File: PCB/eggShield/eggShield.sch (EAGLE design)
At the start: 34 parts, among them U1 V_REG_LDOSMD, U2 V_REG_LDOSMD

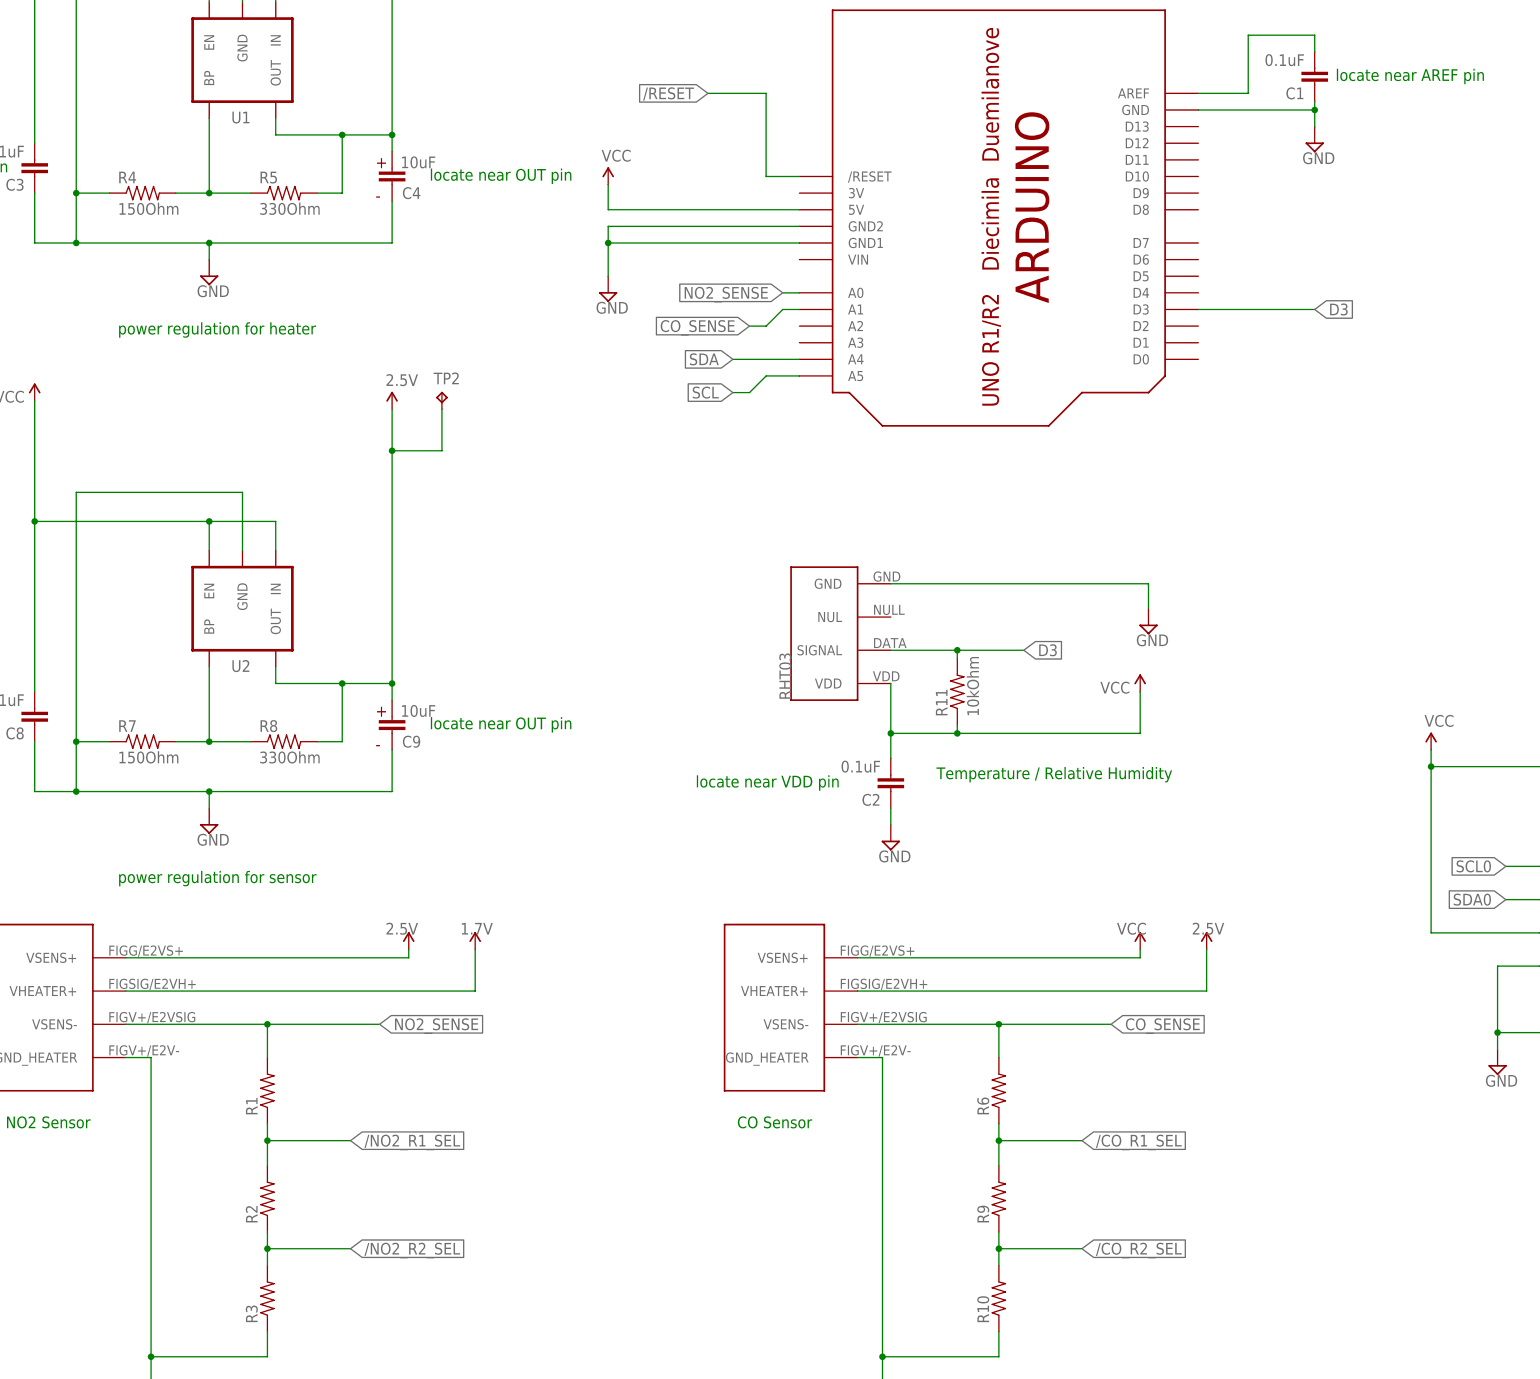
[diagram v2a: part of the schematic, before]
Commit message: added routing for range select signals to arduino header and updated silkscreen for e2v sensors
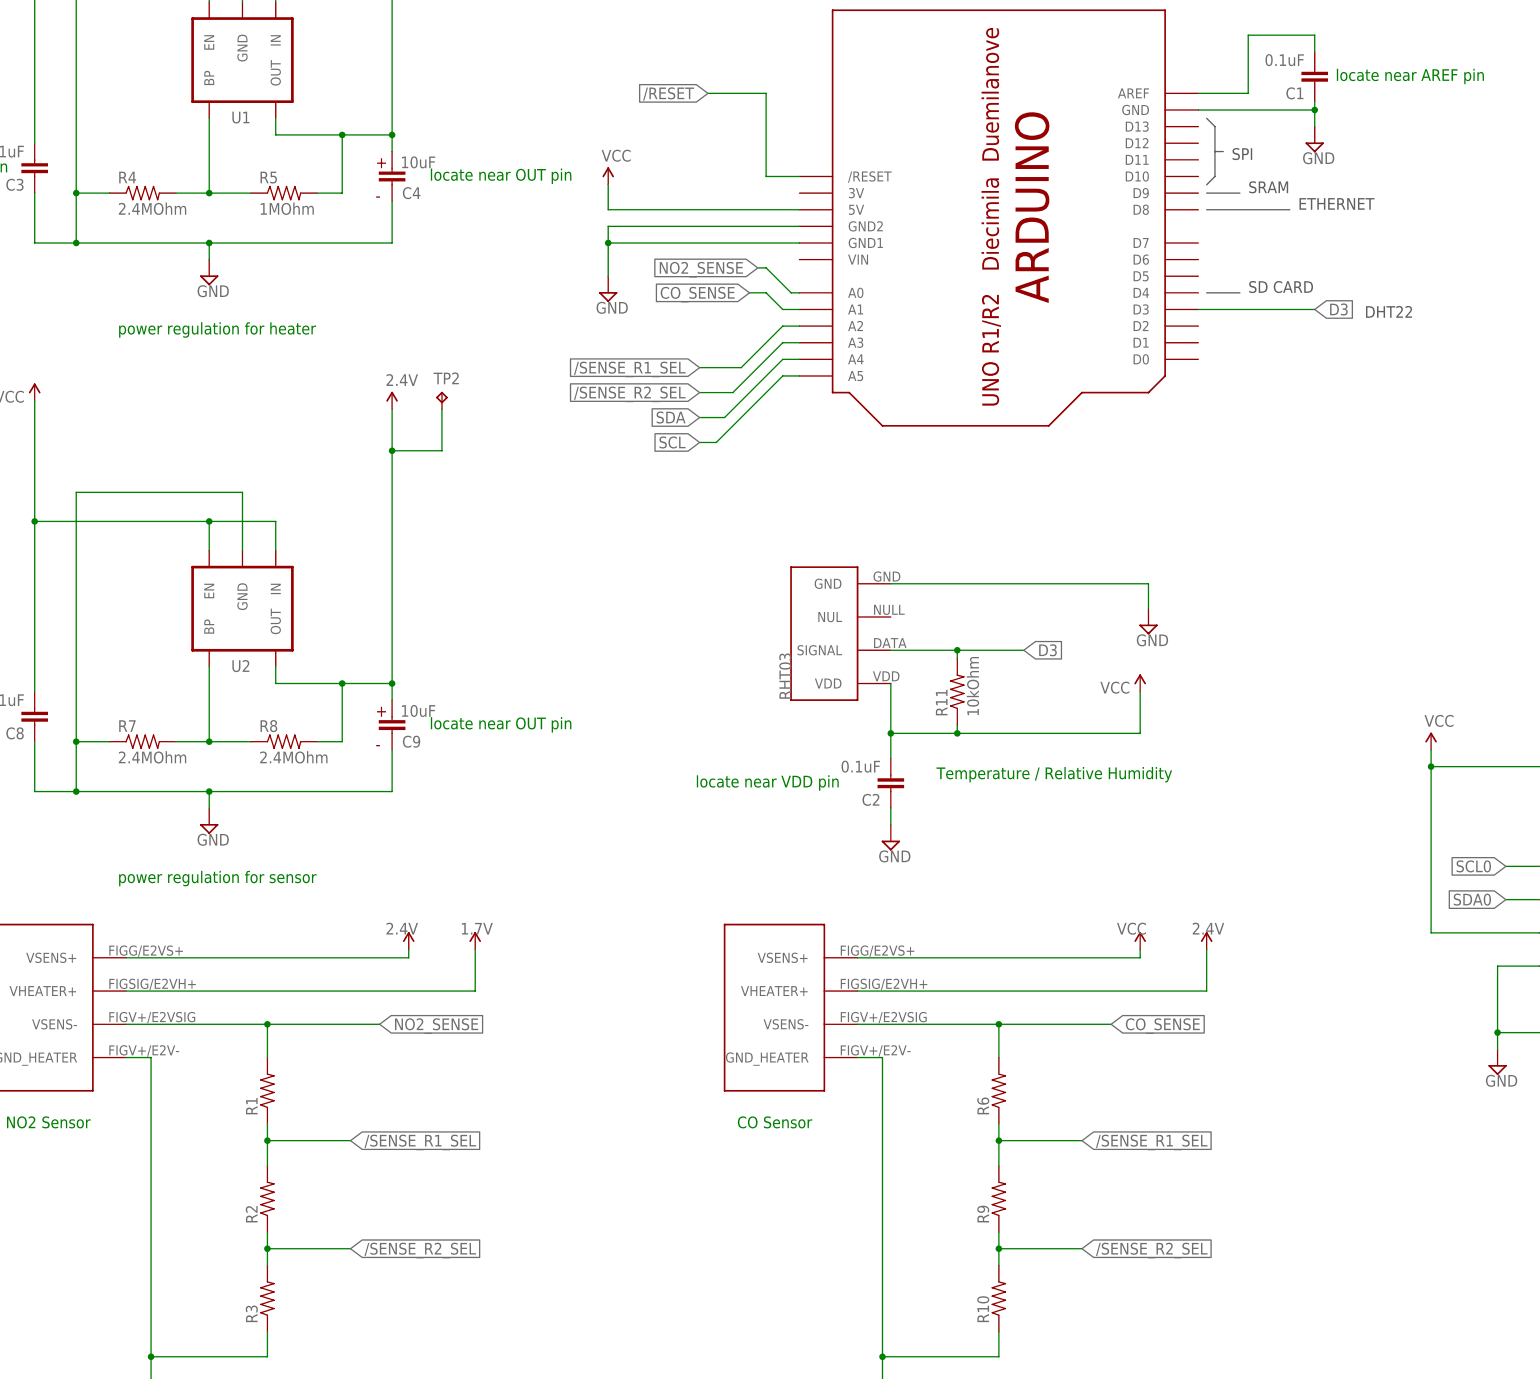
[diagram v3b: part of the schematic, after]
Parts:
- R4, R7: value 150Ohm -> 2.4MOhm
- R5: value 330Ohm -> 1MOhm
- R8: value 330Ohm -> 2.4MOhm
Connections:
- net 2.5V renamed 2.4V
- removed net /CO_R1_SEL: R6.1, R9.2
- removed net /CO_R2_SEL: R10.2, R9.1
- removed net /NO2_R1_SEL: R1.1, R2.2
- removed net /NO2_R2_SEL: R2.1, R3.2
- new net /SENSE_R1_SEL: R1.1, R2.2, R6.1, R9.2, U$7.A2
- new net /SENSE_R2_SEL: R10.2, R2.1, R3.2, R9.1, U$7.A3
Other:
- note added: "DHT22"
- note added: "ETHERNET"
- note added: "SD CARD"
- note added: "SPI"
- note added: "SRAM"
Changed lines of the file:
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@@
 <part name="R1" library="SparkFun" deviceset="RESISTOR" device="0805-RES"/>
 <part name="SUPPLY4" library="supply2" deviceset="GND" device=""/>
-<part name="U$5" library="SparkFun" deviceset="1.8V" device="" value="2.5V"/>
-<part name="R4" library="SparkFun" deviceset="RESISTOR" device="0805-RES" value="150Ohm"/>
-<part name="R5" library="SparkFun" deviceset="RESISTOR" device="0805-RES" value="330Ohm"/>
+<part name="U$5" library="SparkFun" deviceset="1.8V" device="" value="2.4V"/>
+<part name="R4" library="SparkFun" deviceset="RESISTOR" device="0805-RES" value="2.4MOhm"/>
+<part name="R5" library="SparkFun" deviceset="RESISTOR" device="0805-RES" value="1MOhm"/>
 <part name="U1" library="SparkFun" deviceset="V_REG_LDO" device="SMD"/>
 <part name="U$1" library="SparkFun" deviceset="1.8V" device="" value="1.7V"/>
@@
 <part name="R3" library="SparkFun" deviceset="RESISTOR" device="0805-RES"/>
 <part name="SUPPLY9" library="supply2" deviceset="GND" device=""/>
-<part name="2.5V" library="SparkFun" deviceset="1.8V" device="" value="2.5V"/>
+<part name="2.4V" library="SparkFun" deviceset="1.8V" device="" value="2.4V"/>
 <part name="C8" library="SparkFun" deviceset="CAP" device="0603-CAP" value="0.1uF"/>
 <part name="C9" library="wicked-device" deviceset="EEE-1EA100WR" device="" value="10uF"/>
-<part name="R7" library="SparkFun" deviceset="RESISTOR" device="0805-RES" value="150Ohm"/>
-<part name="R8" library="SparkFun" deviceset="RESISTOR" device="0805-RES" value="330Ohm"/>
+<part name="R7" library="SparkFun" deviceset="RESISTOR" device="0805-RES" value="2.4MOhm"/>
+<part name="R8" library="SparkFun" deviceset="RESISTOR" device="0805-RES" value="2.4MOhm"/>
 <part name="U2" library="SparkFun" deviceset="V_REG_LDO" device="SMD"/>
 <part name="CO" library="ricardo" deviceset="E2V" device=""/>
@@
 <part name="SUPPLY6" library="supply2" deviceset="GND" device=""/>
 <part name="U$3" library="SparkFun" deviceset="1.8V" device="" value="VCC"/>
-<part name="U$6" library="SparkFun" deviceset="1.8V" device="" value="2.5V"/>
+<part name="U$6" library="SparkFun" deviceset="1.8V" device="" value="2.4V"/>
 <part name="R9" library="SparkFun" deviceset="RESISTOR" device="0805-RES"/>
 <part name="R10" library="SparkFun" deviceset="RESISTOR" device="0805-RES"/>
@@
 <text x="296.545" y="210.185" size="1.778" layer="91">Do not populate - Nanode has these resistors already</text>
 <text x="296.545" y="206.375" size="1.778" layer="91">This just provides an option for other base boards</text>
+<wire x1="209.55" y1="219.71" x2="210.82" y2="218.44" width="0.1524" layer="97"/>
+<wire x1="210.82" y1="218.44" x2="210.82" y2="214.63" width="0.1524" layer="97"/>
+<wire x1="210.82" y1="214.63" x2="210.82" y2="210.82" width="0.1524" layer="97"/>
+<wire x1="210.82" y1="210.82" x2="209.55" y2="209.55" width="0.1524" layer="97"/>
+<wire x1="210.82" y1="214.63" x2="212.09" y2="214.63" width="0.1524" layer="97"/>
+<wire x1="209.55" y1="208.28" x2="214.63" y2="208.28" width="0.1524" layer="97"/>
+<wire x1="209.55" y1="205.74" x2="222.25" y2="205.74" width="0.1524" layer="97"/>
+<wire x1="209.55" y1="193.04" x2="214.63" y2="193.04" width="0.1524" layer="97"/>
+<text x="213.36" y="213.36" size="1.778" layer="97">SPI</text>
+<text x="215.9" y="208.28" size="1.778" layer="97">SRAM</text>
+<text x="223.52" y="205.74" size="1.778" layer="97">ETHERNET</text>
+<text x="215.9" y="193.04" size="1.778" layer="97">SD CARD</text>
+<text x="233.68" y="189.23" size="1.778" layer="97">DHT22</text>
 </plain>
 <instances>
@@
 <instance part="R3" gate="G$1" x="66.04" y="39.37" rot="R90"/>
 <instance part="SUPPLY9" gate="GND" x="57.15" y="111.76"/>
-<instance part="2.5V" gate="G$1" x="85.09" y="175.26" smashed="yes">
+<instance part="2.4V" gate="G$1" x="85.09" y="175.26" smashed="yes">
 <attribute name="VALUE" x="84.074" y="178.816" size="1.778" layer="96"/>
 </instance>
@@
 </segment>
 </net>
-<net name="/NO2_R1_SEL" class="0">
-<segment>
-<pinref part="R1" gate="G$1" pin="1"/>
-<pinref part="R2" gate="G$1" pin="2"/>
-<wire x1="66.04" y1="66.04" x2="66.04" y2="63.5" width="0.1524" layer="91"/>
-<wire x1="66.04" y1="63.5" x2="66.04" y2="59.69" width="0.1524" layer="91"/>
-<wire x1="66.04" y1="63.5" x2="78.74" y2="63.5" width="0.1524" layer="91"/>
-<junction x="66.04" y="63.5"/>
-<label x="78.74" y="63.5" size="1.778" layer="95" xref="yes"/>
-</segment>
-</net>
-<net name="/NO2_R2_SEL" class="0">
-<segment>
-<pinref part="R2" gate="G$1" pin="1"/>
-<wire x1="66.04" y1="49.53" x2="66.04" y2="46.99" width="0.1524" layer="91"/>
-<pinref part="R3" gate="G$1" pin="2"/>
-<wire x1="66.04" y1="46.99" x2="66.04" y2="44.45" width="0.1524" layer="91"/>
-<wire x1="66.04" y1="46.99" x2="78.74" y2="46.99" width="0.1524" layer="91"/>
-<junction x="66.04" y="46.99"/>
-<label x="78.74" y="46.99" size="1.778" layer="95" xref="yes"/>
-</segment>
-</net>
 <net name="N$1" class="0">
 <segment>
@@
 </segment>
 </net>
-<net name="2.5V" class="0">
-<segment>
-<pinref part="2.5V" gate="G$1" pin="1.8V"/>
+<net name="2.4V" class="0">
+<segment>
+<pinref part="2.4V" gate="G$1" pin="1.8V"/>
 <wire x1="77.47" y1="133.35" x2="85.09" y2="133.35" width="0.1524" layer="91"/>
 <pinref part="C9" gate="G$1" pin="1"/>
@@
 </segment>
 </net>
-<net name="/CO_R1_SEL" class="0">
+<net name="/SENSE_R1_SEL" class="0">
 <segment>
 <pinref part="R6" gate="G$1" pin="1"/>
@@
 <label x="190.5" y="63.5" size="1.778" layer="95" xref="yes"/>
 </segment>
-</net>
-<net name="/CO_R2_SEL" class="0">
+<segment>
+<pinref part="R1" gate="G$1" pin="1"/>
+<pinref part="R2" gate="G$1" pin="2"/>
+<wire x1="66.04" y1="66.04" x2="66.04" y2="63.5" width="0.1524" layer="91"/>
+<wire x1="66.04" y1="63.5" x2="66.04" y2="59.69" width="0.1524" layer="91"/>
+<wire x1="66.04" y1="63.5" x2="78.74" y2="63.5" width="0.1524" layer="91"/>
+<junction x="66.04" y="63.5"/>
+<label x="78.74" y="63.5" size="1.778" layer="95" xref="yes"/>
+</segment>
+<segment>
+<pinref part="U$7" gate="G$1" pin="A2"/>
+<wire x1="147.32" y1="187.96" x2="144.78" y2="187.96" width="0.1524" layer="91"/>
+<wire x1="144.78" y1="187.96" x2="138.43" y2="181.61" width="0.1524" layer="91"/>
+<wire x1="138.43" y1="181.61" x2="132.08" y2="181.61" width="0.1524" layer="91"/>
+<label x="132.08" y="181.61" size="1.778" layer="95" rot="R180" xref="yes"/>
+</segment>
+</net>
+<net name="/SENSE_R2_SEL" class="0">
 <segment>
 <pinref part="R9" gate="G$1" pin="1"/>
@@
 <label x="190.5" y="46.99" size="1.778" layer="95" xref="yes"/>
 </segment>
+<segment>
+<pinref part="R2" gate="G$1" pin="1"/>
+<wire x1="66.04" y1="49.53" x2="66.04" y2="46.99" width="0.1524" layer="91"/>
+<pinref part="R3" gate="G$1" pin="2"/>
+<wire x1="66.04" y1="46.99" x2="66.04" y2="44.45" width="0.1524" layer="91"/>
+<wire x1="66.04" y1="46.99" x2="78.74" y2="46.99" width="0.1524" layer="91"/>
+<junction x="66.04" y="46.99"/>
+<label x="78.74" y="46.99" size="1.778" layer="95" xref="yes"/>
+</segment>
+<segment>
+<pinref part="U$7" gate="G$1" pin="A3"/>
+<wire x1="147.32" y1="185.42" x2="144.78" y2="185.42" width="0.1524" layer="91"/>
+<wire x1="144.78" y1="185.42" x2="137.16" y2="177.8" width="0.1524" layer="91"/>
+<wire x1="137.16" y1="177.8" x2="132.08" y2="177.8" width="0.1524" layer="91"/>
+<label x="132.08" y="177.8" size="1.778" layer="95" rot="R180" xref="yes"/>
+</segment>
 </net>
 <net name="D3" class="0">
@@
 <segment>
 <pinref part="U$7" gate="G$1" pin="A0"/>
-<wire x1="147.32" y1="193.04" x2="144.78" y2="193.04" width="0.1524" layer="91"/>
-<label x="144.78" y="193.04" size="1.778" layer="95" rot="R180" xref="yes"/>
+<wire x1="147.32" y1="193.04" x2="146.05" y2="193.04" width="0.1524" layer="91"/>
+<wire x1="146.05" y1="193.04" x2="142.24" y2="196.85" width="0.1524" layer="91"/>
+<wire x1="142.24" y1="196.85" x2="140.97" y2="196.85" width="0.1524" layer="91"/>
+<label x="140.97" y="196.85" size="1.778" layer="95" rot="R180" xref="yes"/>
 </segment>
 <segment>
@@
 <pinref part="U$7" gate="G$1" pin="A1"/>
 <wire x1="147.32" y1="190.5" x2="144.78" y2="190.5" width="0.1524" layer="91"/>
-<wire x1="144.78" y1="190.5" x2="142.24" y2="187.96" width="0.1524" layer="91"/>
-<wire x1="142.24" y1="187.96" x2="139.7" y2="187.96" width="0.1524" layer="91"/>
-<label x="139.7" y="187.96" size="1.778" layer="95" rot="R180" xref="yes"/>
+<wire x1="144.78" y1="190.5" x2="142.24" y2="193.04" width="0.1524" layer="91"/>
+<wire x1="142.24" y1="193.04" x2="139.7" y2="193.04" width="0.1524" layer="91"/>
+<label x="139.7" y="193.04" size="1.778" layer="95" rot="R180" xref="yes"/>
 </segment>
 <segment>
@@
 <segment>
 <pinref part="U$7" gate="G$1" pin="A4"/>
-<wire x1="147.32" y1="182.88" x2="137.16" y2="182.88" width="0.1524" layer="91"/>
-<label x="137.16" y="182.88" size="1.778" layer="95" rot="R180" xref="yes"/>
+<wire x1="147.32" y1="182.88" x2="144.78" y2="182.88" width="0.1524" layer="91"/>
+<wire x1="144.78" y1="182.88" x2="135.89" y2="173.99" width="0.1524" layer="91"/>
+<wire x1="135.89" y1="173.99" x2="132.08" y2="173.99" width="0.1524" layer="91"/>
+<label x="132.08" y="173.99" size="1.778" layer="95" rot="R180" xref="yes"/>
 </segment>
 <segment>
@@
 <segment>
 <pinref part="U$7" gate="G$1" pin="A5"/>
-<wire x1="147.32" y1="180.34" x2="142.24" y2="180.34" width="0.1524" layer="91"/>
-<wire x1="142.24" y1="180.34" x2="139.7" y2="177.8" width="0.1524" layer="91"/>
-<wire x1="139.7" y1="177.8" x2="137.16" y2="177.8" width="0.1524" layer="91"/>
-<label x="137.16" y="177.8" size="1.778" layer="95" rot="R180" xref="yes"/>
-</segment>
-<segment>
+<wire x1="147.32" y1="180.34" x2="144.78" y2="180.34" width="0.1524" layer="91"/>
+<wire x1="144.78" y1="180.34" x2="134.62" y2="170.18" width="0.1524" layer="91"/>
+<wire x1="134.62" y1="170.18" x2="132.08" y2="170.18" width="0.1524" layer="91"/>
+<label x="132.08" y="170.18" size="1.778" layer="95" rot="R180" xref="yes"/>
+</segment>
+<segment>
